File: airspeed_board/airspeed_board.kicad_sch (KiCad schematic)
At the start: 6 parts, among them J1 BME280, J2 ADXL345, J3 MPXV5002DP, U1 ESP32-C3_SUPERMINI, U2 XGZP6897D_1, U3 XGZP6897D_2

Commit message: updated board layout
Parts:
- removed J3: MPXV5002DP, Connector_PinHeader_2.54mm:PinHeader_1x03_P2.54mm_Vertical, symbol Connector:Conn_01x03_Pin
- added C1: 0.1uF, Capacitor_SMD:C_0805_2012Metric, symbol Device:C
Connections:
- net 3.3V: now also J1.1 (Pin_1), J2.2 (Pin_2), C1.2
- net GND: now also J1.2 (Pin_2), J2.1 (Pin_1), C1.1
- net SCL: now also J1.3 (Pin_3), J2.8 (Pin_8)
- net SDA: now also J1.4 (Pin_4), J2.7 (Pin_7)
- net 5V: now reaches U1.5V
- no-connect marks 0 -> 17
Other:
- moved on the sheet: U2

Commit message: updates to pcb
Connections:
- net SCL: no longer U3.7 (SCL)
- net SDA: no longer U3.6 (SDA)
- net SDA2: now reaches U1.20 (GPIO20)
- net SDA2: now also U3.6 (SDA)
- net SCL2: now reaches U1.21 (GPIO21)
- net SCL2: now also U3.7 (SCL)
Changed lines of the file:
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@@
   (junction (at 193.04 36.83) (diameter 0) (color 0 0 0 0)
-  )
-  (junction (at 193.04 57.15) (diameter 0) (color 0 0 0 0)
   )
   (no_connect (at 102.87 77.47))
@@
   (no_connect (at 138.43 82.55))
   (no_connect (at 74.93 87.63))
-  (wire (pts (xy 170.18 57.15) (xy 193.04 57.15))
-    (stroke (width 0) (type default))
-  )
   (wire (pts (xy 193.04 57.15) (xy 193.04 44.45))
     (stroke (width 0) (type default))
   )
   (wire (pts (xy 193.04 36.83) (xy 205.74 36.83))
-    (stroke (width 0) (type default))
-  )
-  (wire (pts (xy 193.04 59.69) (xy 193.04 57.15))
-    (stroke (width 0) (type default))
-  )
-  (wire (pts (xy 193.04 57.15) (xy 205.74 57.15))
     (stroke (width 0) (type default))
   )
@@
     )
   )
-  (global_label "SDA" (shape input) (at 213.36 46.99 0) (fields_autoplaced)
+  (global_label "SDA2" (shape input) (at 213.36 46.99 0) (fields_autoplaced)
     (effects (font (size 1.27 1.27)) (justify left))
-    (property "Intersheetrefs" "${INTERSHEET_REFS}" (at 219.9133 46.99 0)
+    (property "Intersheetrefs" "${INTERSHEET_REFS}" (at 221.1228 46.99 0)
       (effects (font (size 1.27 1.27)) (justify left) hide)
     )
@@
     )
   )
-  (global_label "SCL" (shape input) (at 213.36 44.45 0) (fields_autoplaced)
+  (global_label "SCL2" (shape input) (at 213.36 44.45 0) (fields_autoplaced)
     (effects (font (size 1.27 1.27)) (justify left))
-    (property "Intersheetrefs" "${INTERSHEET_REFS}" (at 219.8528 44.45 0)
+    (property "Intersheetrefs" "${INTERSHEET_REFS}" (at 221.0623 44.45 0)
       (effects (font (size 1.27 1.27)) (justify left) hide)
     )
@@
     (effects (font (size 1.27 1.27)) (justify left))
     (property "Intersheetrefs" "${INTERSHEET_REFS}" (at 184.3533 46.99 0)
+      (effects (font (size 1.27 1.27)) (justify left) hide)
+    )
+  )
+  (global_label "SCL2" (shape input) (at 138.43 85.09 0) (fields_autoplaced)
+    (effects (font (size 1.27 1.27)) (justify left))
+    (property "Intersheetrefs" "${INTERSHEET_REFS}" (at 146.1323 85.09 0)
       (effects (font (size 1.27 1.27)) (justify left) hide)
     )
@@
     )
   )
+  (global_label "SDA2" (shape input) (at 138.43 82.55 0) (fields_autoplaced)
+    (effects (font (size 1.27 1.27)) (justify left))
+    (property "Intersheetrefs" "${INTERSHEET_REFS}" (at 146.1928 82.55 0)
+      (effects (font (size 1.27 1.27)) (justify left) hide)
+    )
+  )
   (global_label "SCL" (shape input) (at 74.93 92.71 0) (fields_autoplaced)
     (effects (font (size 1.27 1.27)) (justify left))
@@
     )
   )
+  (global_label "GND" (shape input) (at 193.04 57.15 270) (fields_autoplaced)
+    (effects (font (size 1.27 1.27)) (justify right))
+    (property "Intersheetrefs" "${INTERSHEET_REFS}" (at 193.04 64.0057 90)
+      (effects (font (size 1.27 1.27)) (justify right) hide)
+    )
+  )
   (global_label "GND" (shape input) (at 74.93 54.61 0) (fields_autoplaced)
     (effects (font (size 1.27 1.27)) (justify left))
     (property "Intersheetrefs" "${INTERSHEET_REFS}" (at 81.7857 54.61 0)
       (effects (font (size 1.27 1.27)) (justify left) hide)
+    )
+  )
+  (global_label "GND" (shape input) (at 205.74 57.15 270) (fields_autoplaced)
+    (effects (font (size 1.27 1.27)) (justify right))
+    (property "Intersheetrefs" "${INTERSHEET_REFS}" (at 205.74 64.0057 90)
+      (effects (font (size 1.27 1.27)) (justify right) hide)
     )
   )
@@
     )
   )
-  (global_label "GND" (shape input) (at 193.04 59.69 270) (fields_autoplaced)
+  (global_label "GND" (shape input) (at 170.18 57.15 270) (fields_autoplaced)
     (effects (font (size 1.27 1.27)) (justify right))
-    (property "Intersheetrefs" "${INTERSHEET_REFS}" (at 193.04 66.5457 90)
+    (property "Intersheetrefs" "${INTERSHEET_REFS}" (at 170.18 64.0057 90)
       (effects (font (size 1.27 1.27)) (justify right) hide)
     )

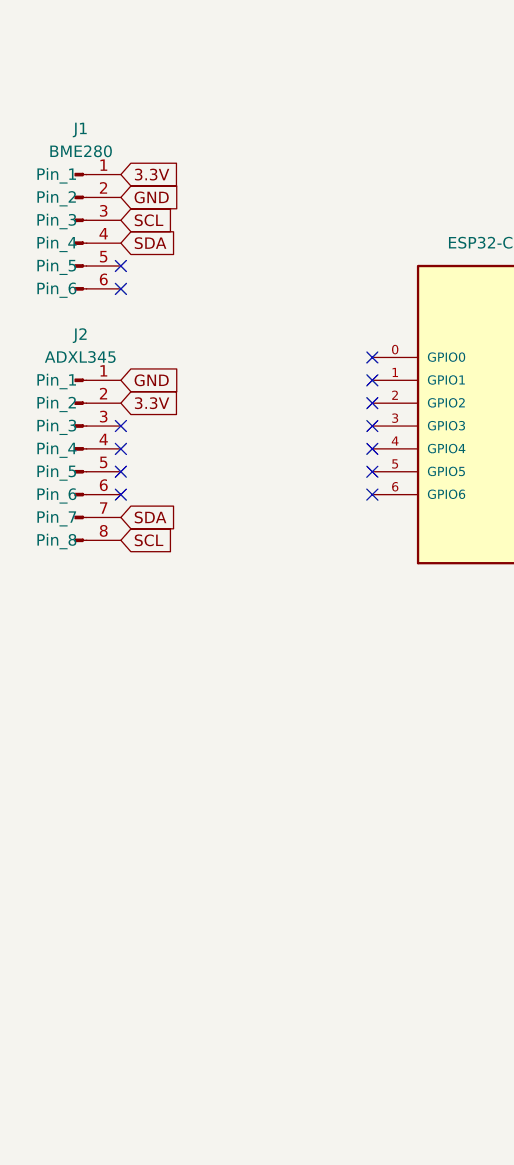
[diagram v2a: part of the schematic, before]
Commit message: update fix the power for bme and battery connector
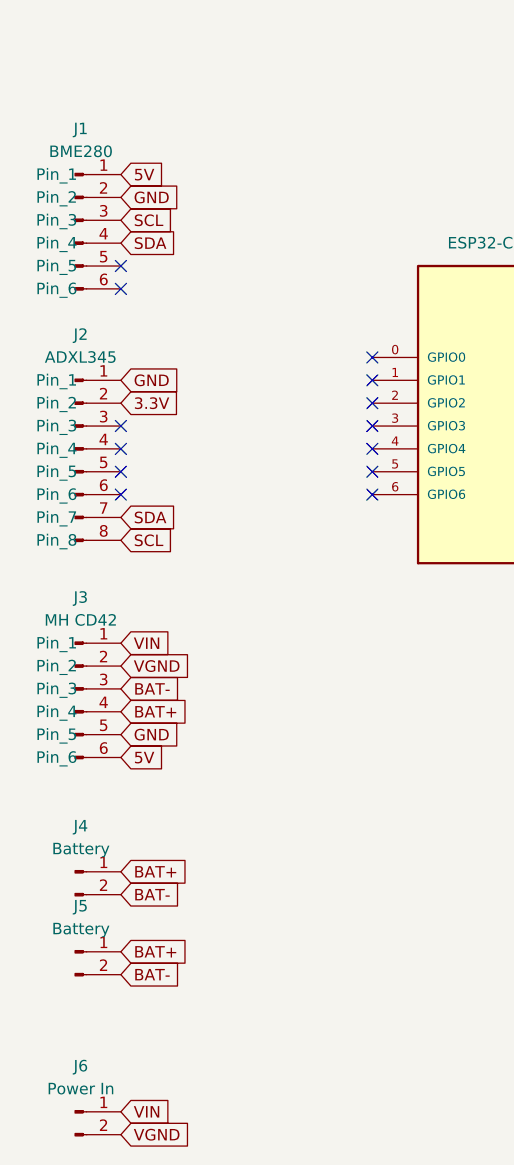
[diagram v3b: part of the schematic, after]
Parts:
- added J3: MH CD42, Connector_PinHeader_2.54mm:PinHeader_1x06_P2.54mm_Vertical, symbol Connector:Conn_01x06_Pin
- added J4: Battery, Connector_PinSocket_2.54mm:PinSocket_1x02_P2.54mm_Vertical, symbol Connector:Conn_01x02_Pin
- added J5: Battery, Connector_PinSocket_1.27mm:PinSocket_1x02_P1.27mm_Vertical, symbol Connector:Conn_01x02_Pin
- added J6: Power In, Connector_PinHeader_2.54mm:PinHeader_1x02_P2.54mm_Vertical, symbol Connector:Conn_01x02_Pin
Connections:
- net 3.3V: no longer J1.1 (Pin_1)
- net 5V: now also J1.1 (Pin_1), J3.6 (Pin_6)
- net GND: now also J3.5 (Pin_5)
- new net BAT+: J3.4 (Pin_4), J4.1 (Pin_1), J5.1 (Pin_1)
- new net BAT-: J3.3 (Pin_3), J4.2 (Pin_2), J5.2 (Pin_2)
- new net VGND: J3.2 (Pin_2), J6.2 (Pin_2)
- new net VIN: J3.1 (Pin_1), J6.1 (Pin_1)
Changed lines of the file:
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@@
     (stroke (width 0) (type default))
   )
+  (global_label "BAT-" (shape input) (at 74.93 140.97 0) (fields_autoplaced)
+    (effects (font (size 1.27 1.27)) (justify left))
+    (property "Intersheetrefs" "${INTERSHEET_REFS}" (at 82.8138 140.97 0)
+      (effects (font (size 1.27 1.27)) (justify left) hide)
+    )
+  )
   (global_label "3.3V" (shape input) (at 138.43 67.31 0) (fields_autoplaced)
     (effects (font (size 1.27 1.27)) (justify left))
@@
     )
   )
+  (global_label "BAT+" (shape input) (at 74.93 111.76 0) (fields_autoplaced)
+    (effects (font (size 1.27 1.27)) (justify left))
+    (property "Intersheetrefs" "${INTERSHEET_REFS}" (at 82.8138 111.76 0)
+      (effects (font (size 1.27 1.27)) (justify left) hide)
+    )
+  )
+  (global_label "BAT-" (shape input) (at 74.93 132.08 0) (fields_autoplaced)
+    (effects (font (size 1.27 1.27)) (justify left))
+    (property "Intersheetrefs" "${INTERSHEET_REFS}" (at 82.8138 132.08 0)
+      (effects (font (size 1.27 1.27)) (justify left) hide)
+    )
+  )
   (global_label "SDA2" (shape input) (at 213.36 46.99 0) (fields_autoplaced)
     (effects (font (size 1.27 1.27)) (justify left))
@@
     )
   )
+  (global_label "BAT+" (shape input) (at 74.93 138.43 0) (fields_autoplaced)
+    (effects (font (size 1.27 1.27)) (justify left))
+    (property "Intersheetrefs" "${INTERSHEET_REFS}" (at 82.8138 138.43 0)
+      (effects (font (size 1.27 1.27)) (justify left) hide)
+    )
+  )
+  (global_label "5V" (shape input) (at 74.93 116.84 0) (fields_autoplaced)
+    (effects (font (size 1.27 1.27)) (justify left))
+    (property "Intersheetrefs" "${INTERSHEET_REFS}" (at 80.2133 116.84 0)
+      (effects (font (size 1.27 1.27)) (justify left) hide)
+    )
+  )
+  (global_label "VGND" (shape input) (at 74.93 106.68 0) (fields_autoplaced)
+    (effects (font (size 1.27 1.27)) (justify left))
+    (property "Intersheetrefs" "${INTERSHEET_REFS}" (at 82.8743 106.68 0)
+      (effects (font (size 1.27 1.27)) (justify left) hide)
+    )
+  )
   (global_label "SCL2" (shape input) (at 138.43 85.09 0) (fields_autoplaced)
     (effects (font (size 1.27 1.27)) (justify left))
@@
     )
   )
+  (global_label "5V" (shape input) (at 74.93 52.07 0) (fields_autoplaced)
+    (effects (font (size 1.27 1.27)) (justify left))
+    (property "Intersheetrefs" "${INTERSHEET_REFS}" (at 80.2133 52.07 0)
+      (effects (font (size 1.27 1.27)) (justify left) hide)
+    )
+  )
   (global_label "SCL" (shape input) (at 74.93 57.15 0) (fields_autoplaced)
     (effects (font (size 1.27 1.27)) (justify left))
@@
     )
   )
+  (global_label "VIN" (shape input) (at 74.93 156.21 0) (fields_autoplaced)
+    (effects (font (size 1.27 1.27)) (justify left))
+    (property "Intersheetrefs" "${INTERSHEET_REFS}" (at 80.9391 156.21 0)
+      (effects (font (size 1.27 1.27)) (justify left) hide)
+    )
+  )
   (global_label "GND" (shape input) (at 74.93 74.93 0) (fields_autoplaced)
     (effects (font (size 1.27 1.27)) (justify left))
     (property "Intersheetrefs" "${INTERSHEET_REFS}" (at 81.7857 74.93 0)
-      (effects (font (size 1.27 1.27)) (justify left) hide)
-    )
-  )
-  (global_label "3.3V" (shape input) (at 74.93 52.07 0) (fields_autoplaced)
-    (effects (font (size 1.27 1.27)) (justify left))
-    (property "Intersheetrefs" "${INTERSHEET_REFS}" (at 82.0276 52.07 0)
       (effects (font (size 1.27 1.27)) (justify left) hide)
     )
@@
     )
   )
+  (global_label "VGND" (shape input) (at 74.93 158.75 0) (fields_autoplaced)
+    (effects (font (size 1.27 1.27)) (justify left))
+    (property "Intersheetrefs" "${INTERSHEET_REFS}" (at 82.8743 158.75 0)
+      (effects (font (size 1.27 1.27)) (justify left) hide)
+    )
+  )
   (global_label "3.3V" (shape input) (at 74.93 77.47 0) (fields_autoplaced)
     (effects (font (size 1.27 1.27)) (justify left))
@@
     )
   )
+  (global_label "BAT-" (shape input) (at 74.93 109.22 0) (fields_autoplaced)
+    (effects (font (size 1.27 1.27)) (justify left))
+    (property "Intersheetrefs" "${INTERSHEET_REFS}" (at 82.8138 109.22 0)
+      (effects (font (size 1.27 1.27)) (justify left) hide)
+    )
+  )
+  (global_label "GND" (shape input) (at 74.93 114.3 0) (fields_autoplaced)
+    (effects (font (size 1.27 1.27)) (justify left))
+    (property "Intersheetrefs" "${INTERSHEET_REFS}" (at 81.7857 114.3 0)
+      (effects (font (size 1.27 1.27)) (justify left) hide)
+    )
+  )
   (global_label "SDA" (shape input) (at 138.43 74.93 0) (fields_autoplaced)
     (effects (font (size 1.27 1.27)) (justify left))
@@
     (effects (font (size 1.27 1.27)) (justify left))
     (property "Intersheetrefs" "${INTERSHEET_REFS}" (at 81.4833 90.17 0)
+      (effects (font (size 1.27 1.27)) (justify left) hide)
+    )
+  )
+  (global_label "VIN" (shape input) (at 74.93 104.14 0) (fields_autoplaced)
+    (effects (font (size 1.27 1.27)) (justify left))
+    (property "Intersheetrefs" "${INTERSHEET_REFS}" (at 80.9391 104.14 0)
       (effects (font (size 1.27 1.27)) (justify left) hide)
     )
@@
     )
   )
+  (global_label "BAT+" (shape input) (at 74.93 129.54 0) (fields_autoplaced)
+    (effects (font (size 1.27 1.27)) (justify left))
+    (property "Intersheetrefs" "${INTERSHEET_REFS}" (at 82.8138 129.54 0)
+      (effects (font (size 1.27 1.27)) (justify left) hide)
+    )
+  )
   (global_label "5V" (shape input) (at 138.43 64.77 0) (fields_autoplaced)
     (effects (font (size 1.27 1.27)) (justify left))
     (property "Intersheetrefs" "${INTERSHEET_REFS}" (at 143.7133 64.77 0)
       (effects (font (size 1.27 1.27)) (justify left) hide)
+    )
+  )
+  (symbol (lib_id "Connector:Conn_01x02_Pin") (at 69.85 156.21 0) (unit 1)
+    (in_bom yes) (on_board yes) (dnp no) (fields_autoplaced)
+    (property "Reference" "J6" (at 70.485 151.13 0)
+      (effects (font (size 1.27 1.27)))
+    )
+    (property "Value" "Power In" (at 70.485 153.67 0)
+      (effects (font (size 1.27 1.27)))
+    )
+    (property "Footprint" "Connector_PinHeader_2.54mm:PinHeader_1x02_P2.54mm_Vertical" (at 69.85 156.21 0)
+      (effects (font (size 1.27 1.27)) hide)
+    )
+    (property "Datasheet" "~" (at 69.85 156.21 0)
+      (effects (font (size 1.27 1.27)) hide)
+    )
+    (pin "1")
+    (pin "2")
+    (instances
+      (project "airspeed_board"
+        (path "/0a28f27d-d548-4aad-94f9-325f9556760e"
+          (reference "J6") (unit 1)
+        )
+      )
     )
   )
@@
     )
   )
+  (symbol (lib_name "Conn_01x06_Pin_1") (lib_id "Connector:Conn_01x06_Pin") (at 69.85 109.22 0) (unit 1)
+    (in_bom yes) (on_board yes) (dnp no) (fields_autoplaced)
+    (property "Reference" "J3" (at 70.485 99.06 0)
+      (effects (font (size 1.27 1.27)))
+    )
+    (property "Value" "MH CD42" (at 70.485 101.6 0)
+      (effects (font (size 1.27 1.27)))
+    )
+    (property "Footprint" "Connector_PinHeader_2.54mm:PinHeader_1x06_P2.54mm_Vertical" (at 69.85 109.22 0)
+      (effects (font (size 1.27 1.27)) hide)
+    )
+    (property "Datasheet" "~" (at 69.85 109.22 0)
+      (effects (font (size 1.27 1.27)) hide)
+    )
+    (pin "1")
+    (pin "2")
+    (pin "3")
+    (pin "4")
+    (pin "5")
+    (pin "6")
+    (instances
+      (project "airspeed_board"
+        (path "/0a28f27d-d548-4aad-94f9-325f9556760e"
+          (reference "J3") (unit 1)
+        )
+      )
+    )
+  )
   (symbol (lib_id "Connector:Conn_01x08_Pin") (at 69.85 82.55 0) (unit 1)
     (in_bom yes) (on_board yes) (dnp no) (fields_autoplaced)
@@
         )
       )
+    )
+  )
+  (symbol (lib_id "Connector:Conn_01x02_Pin") (at 69.85 138.43 0) (unit 1)
+    (in_bom yes) (on_board yes) (dnp no) (fields_autoplaced)
+    (property "Reference" "J5" (at 70.485 133.35 0)
+      (effects (font (size 1.27 1.27)))
+    )
+    (property "Value" "Battery" (at 70.485 135.89 0)
+      (effects (font (size 1.27 1.27)))
+    )
+    (property "Footprint" "Connector_PinSocket_1.27mm:PinSocket_1x02_P1.27mm_Vertical" (at 69.85 138.43 0)
+      (effects (font (size 1.27 1.27)) hide)
+    )
+    (property "Datasheet" "~" (at 69.85 138.43 0)
+      (effects (font (size 1.27 1.27)) hide)
+    )
+    (pin "1")
+    (pin "2")
+    (instances
+      (project "airspeed_board"
+        (path "/0a28f27d-d548-4aad-94f9-325f9556760e"
+          (reference "J5") (unit 1)
+        )
+      )
+    )
+  )
+  (symbol (lib_id "Connector:Conn_01x02_Pin") (at 69.85 129.54 0) (unit 1)
+    (in_bom yes) (on_board yes) (dnp no) (fields_autoplaced)
+    (property "Reference" "J4" (at 70.485 124.46 0)
+      (effects (font (size 1.27 1.27)))
+    )
+    (property "Value" "Battery" (at 70.485 127 0)
+      (effects (font (size 1.27 1.27)))
+    )
+    (property "Footprint" "Connector_PinSocket_2.54mm:PinSocket_1x02_P2.54mm_Vertical" (at 69.85 129.54 0)
+      (effects (font (size 1.27 1.27)) hide)
+    )
+    (property "Datasheet" "~" (at 69.85 129.54 0)
+      (effects (font (size 1.27 1.27)) hide)
+    )
+    (pin "1")
+    (pin "2")
+    (instances
+      (project "airspeed_board"
+        (path "/0a28f27d-d548-4aad-94f9-325f9556760e"
+          (reference "J4") (unit 1)
+        )
+      )
